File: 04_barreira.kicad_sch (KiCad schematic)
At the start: 2 parts, among them U5 ISO7141CCDBQR

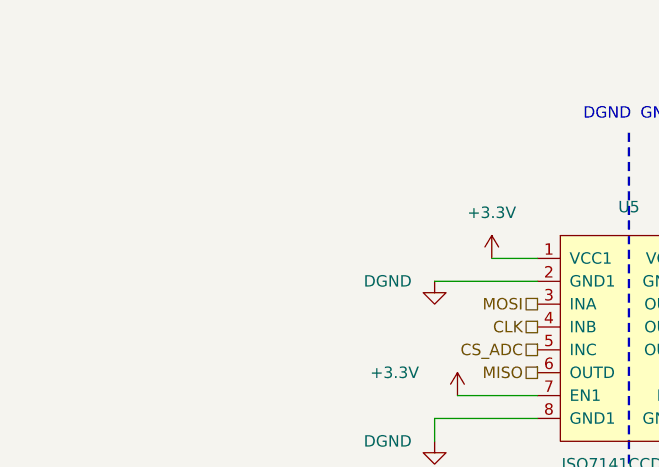
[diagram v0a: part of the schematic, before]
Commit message: Esquematico: alimentacao do lado PLC passa da folha 3 para a folha 4
U2 (MCP1824, +3.3V do lado DGND), C6, C8, C9, T3 e T5 desenhados na
folha 4 (barreira digital), junto ao ISO7141 que alimentam. Limpeza
grafica nas folhas 2 e 6 (rectangulos e fios soltos).

Sem mudanca electrica: netlist com os mesmos 148 componentes e nenhum
pino com rede diferente; ERC 0 erros; DRC 0 erros, paridade 0.

Co-Authored-By: Claude Opus 5.5 (1M context) <noreply@anthropic.com>
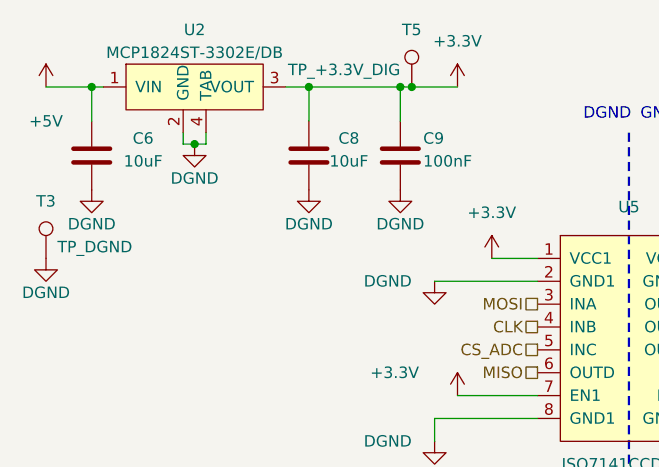
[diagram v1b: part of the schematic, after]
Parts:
- added C6, C8: 10uF, EBM7_V23:0603C, symbol Device:C
- added C9: 100nF, EBM7_V23:0603C, symbol Device:C
- added T3: TP_DGND, EBM7_V23:TestPad_Via, symbol Connector:TestPoint
- added T5: TP_+3.3V_DIG, EBM7_V23:TestPad_Via, symbol Connector:TestPoint
- added U2: MCP1824ST-3302E/DB, EBM7_V23:SOT-223-3, symbol EBM7_V23_proyecto2:MCP1824ST-3302E
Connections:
- net +3.3V: now also C8.2, C9.1, T5.1, U2.3 (VOUT)
- net DGND: now also C6.1, C8.1, C9.2, T3.1, U2.2 (GND), U2.4 (TAB)
- new net +5V: C6.2, U2.1 (VIN)
